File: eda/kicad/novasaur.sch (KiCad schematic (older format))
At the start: 30 parts, among them J9 RAM, SW1 RESET, U1 74F86, U10 74F574, U11 74F574, U12 ATF16V8B, U2 74F08, U3 74F32, U4 74ALS139, U5 74ALS139, U6 74F157, U7 74F175, U8 74F574, U9 74F138, X1 33M

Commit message: power sw + super caps
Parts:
- removed J9: RAM, Connector_PinHeader_2.54mm:PinHeader_1x03_P2.54mm_Vertical, symbol Connector_Generic:Conn_01x03
- removed R1: 1k, Resistor_THT:R_Axial_DIN0204_L3.6mm_D1.6mm_P7.62mm_Horizontal, symbol Device:R_US
- removed SW1: RESET, FSMRA3JH04:SWITCH_FSMRA3JH04, symbol novasaur-rescue:SW_Push-Switch
- TP28: value ILCP -> CLCP
- TP29: value IHCP -> CHCP
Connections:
- net DA17: now also U6.7 (Zb)
- net I0 renamed C0
- net I1 renamed C1
- net I10 renamed C10
- net I11 renamed C11
- net I12 renamed C12
- net I13 renamed C13
- net I14 renamed C14
- net I15 renamed C15
- net I2 renamed C2
- net I3 renamed C3
- net I4 renamed C4
- net I5 renamed C5
- net I6 renamed C6
- net I7 renamed C7
- net I8 renamed C8
- net I9 renamed C9
- net ccp renamed tcp
- net ~inoe renamed ~ioe
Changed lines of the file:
@@
 Sheet 1 4
 Title "Novasaur Retrocomputer"
-Date "2020-03-31"
+Date "2020-05-02"
 Rev "1.6"
 Comp ""
@@
 Wire Wire Line
 	4250 6000 4250 6550
-$Comp
-L novasaur-rescue:SW_Push-Switch SW1
-U 1 1 5E0603B4
-P 3650 1500
-AR Path="/5E0603B4" Ref="SW1"  Part="1"
-AR Path="/5CDEEC9F/5E0603B4" Ref="SW?"  Part="1"
-AR Path="/62D13D9D/5E0603B4" Ref="SW?"  Part="1"
-AR Path="/5DAA5CD8/5E0603B4" Ref="SW?"  Part="1"
-F 0 "SW1" H 3600 1850 50  0000 L CNN
-F 1 "RESET" H 3550 1750 50  0000 L CNN
-F 2 "FSMRA3JH04:SWITCH_FSMRA3JH04" H 3650 1700 50  0001 C CNN
-F 3 "~" H 3650 1700 50  0001 C CNN
-	1    3650 1500
-	-1   0    0    -1
-$EndComp
 Text GLabel 1350 1800 0    50   Output ~ 0
 alu
@@
 pcent
 Text Label 2500 1700 0    50   ~ 0
-I12
+C12
 Entry Wire Line
 	2650 1700 2750 1800
-Text GLabel 2750 1600 2    50   Input ~ 0
+Text GLabel 3050 1600 2    50   Input ~ 0
 DD[0..7]
 Wire Wire Line
@@
 $EndComp
 Text Label 2550 3200 0    50   ~ 0
-I8
+C8
 Text Label 2550 3300 0    50   ~ 0
-I9
+C9
 Text Label 2550 3400 0    50   ~ 0
-I0
+C0
 Text Label 2500 1900 0    50   ~ 0
-I14
+C14
 Text GLabel 2750 6000 3    50   Output ~ 0
-I[0..15]
+C[0..15]
 Entry Wire Line
 	2650 3200 2750 3300
@@
 	4450 5800 4350 5700
 Text Label 2550 5000 0    50   ~ 0
-I8
+C8
 Text Label 2550 5100 0    50   ~ 0
-I9
+C9
 Text Label 2500 5200 0    50   ~ 0
-I10
+C10
 Text Label 2500 5300 0    50   ~ 0
-I11
+C11
 Text Label 2500 5400 0    50   ~ 0
-I12
+C12
 Text Label 2500 5500 0    50   ~ 0
-I13
+C13
 Text Label 2500 5600 0    50   ~ 0
-I14
+C14
 Text Label 2500 5700 0    50   ~ 0
-I15
+C15
 Text Label 4200 5000 0    50   ~ 0
 PD0
@@
 	2650 1900 2750 2000
 Text Label 2500 1800 0    50   ~ 0
-I13
+C13
 Entry Wire Line
 	2650 1800 2750 1900
@@
 PD0
 Text Label 2850 5700 0    50   ~ 0
-I7
+C7
 Text Label 2850 5600 0    50   ~ 0
-I6
+C6
 Text Label 2850 5500 0    50   ~ 0
-I5
+C5
 Text Label 2850 5400 0    50   ~ 0
-I4
+C4
 Text Label 2850 5300 0    50   ~ 0
-I3
+C3
 Text Label 2850 5200 0    50   ~ 0
-I2
+C2
 Text Label 2850 5100 0    50   ~ 0
-I1
+C1
 Text Label 2850 5000 0    50   ~ 0
-I0
+C0
 Entry Wire Line
 	2750 5800 2650 5700
@@
 	1150 5000 1050 4900
 Text Label 2550 3700 0    50   ~ 0
-I1
+C1
 Text GLabel 1350 3900 0    50   Output ~ 0
 pgcp
@@
 $EndComp
 Text Label 2500 2000 0    50   ~ 0
-I15
+C15
 Entry Wire Line
 	2750 4650 2850 4550
@@
 	2850 4650 3050 4650
 Text Label 2850 4650 0    50   ~ 0
-I0
+C0
 Text Label 2850 4550 0    50   ~ 0
-I1
+C1
 Text Label 2850 4450 0    50   ~ 0
-I2
+C2
 Text Label 2850 4350 0    50   ~ 0
-I3
+C3
 Text Label 2850 4250 0    50   ~ 0
-I4
+C4
 Text Label 2850 4150 0    50   ~ 0
-I5
+C5
 Text Label 2850 4050 0    50   ~ 0
-I6
+C6
 Text Label 2850 3950 0    50   ~ 0
-I7
+C7
 $Comp
 L power:VCC #PWR?
@@
 ~exec
 Text GLabel 9300 1700 2    50   Output ~ 0
-ccp
+tcp
 Text GLabel 6900 2300 0    50   Input ~ 0
 hblank
@@
 	1    0    0    -1
 $EndComp
-$Comp
-L power:GNDD #PWR?
-U 1 1 5DEF95A1
-P 4150 1650
-AR Path="/5CDEEC9F/5DEF95A1" Ref="#PWR?"  Part="1"
-AR Path="/5DAA5CD8/5DEF95A1" Ref="#PWR?"  Part="1"
-AR Path="/5DEF95A1" Ref="#PWR0194"  Part="1"
-F 0 "#PWR0194" H 4150 1400 50  0001 C CNN
-F 1 "GNDD" H 4154 1495 50  0000 C CNN
-F 2 "" H 4150 1650 50  0001 C CNN
-F 3 "" H 4150 1650 50  0001 C CNN
-	1    4150 1650
-	1    0    0    -1
-$EndComp
-Wire Wire Line
-	4150 1550 4150 1650
-Wire Wire Line
-	4000 1600 4000 1550
-Wire Wire Line
-	4000 1500 3950 1500
-Wire Wire Line
-	4000 1550 4150 1550
-Connection ~ 4000 1550
-Wire Wire Line
-	4000 1550 4000 1500
-Text Label 2500 1600 0    50   ~ 0
+Text Label 2850 1600 0    50   ~ 0
 DD7
-$Comp
-L Device:R_US R?
-U 1 1 5E523FD1
-P 3050 1300
-AR Path="/62D13D9D/5E523FD1" Ref="R?"  Part="1"
-AR Path="/5DAA19D5/5E523FD1" Ref="R?"  Part="1"
-AR Path="/5DAA5CD8/5D99DA9F/5E523FD1" Ref="R?"  Part="1"
-AR Path="/5DA1E9BA/5E523FD1" Ref="R?"  Part="1"
-AR Path="/5E523FD1" Ref="R1"  Part="1"
-F 0 "R1" H 3150 1350 50  0000 L CNN
-F 1 "1k" H 3150 1250 50  0000 L CNN
-F 2 "Resistor_THT:R_Axial_DIN0204_L3.6mm_D1.6mm_P7.62mm_Horizontal" V 3090 1290 50  0001 C CNN
-F 3 "~" H 3050 1300 50  0001 C CNN
-	1    3050 1300
-	1    0    0    -1
-$EndComp
-$Comp
-L power:VCC #PWR?
-U 1 1 5E54FDAD
-P 3050 1100
-AR Path="/5CDEEC9F/5E54FDAD" Ref="#PWR?"  Part="1"
-AR Path="/5DAA5CD8/5E54FDAD" Ref="#PWR?"  Part="1"
-AR Path="/5E54FDAD" Ref="#PWR0111"  Part="1"
-F 0 "#PWR0111" H 3050 950 50  0001 C CNN
-F 1 "VCC" H 3067 1273 50  0000 C CNN
-F 2 "" H 3050 1100 50  0001 C CNN
-F 3 "" H 3050 1100 50  0001 C CNN
-	1    3050 1100
-	1    0    0    -1
-$EndComp
-Wire Wire Line
-	3050 1500 3050 1450
-Wire Wire Line
-	3050 1150 3050 1100
 Wire Wire Line
 	9600 1100 8000 1100
@@
 	2850 3200 3150 3200
 Text Label 2850 3100 0    50   ~ 0
-I3
+C3
 Text GLabel 3150 3400 0    50   Input ~ 0
 ~read
@@
 acp
 Text GLabel 4150 3100 2    50   Output ~ 0
-~inoe
+~ioe
 Entry Wire Line
 	2850 2200 2750 2300
 Text Label 2850 2200 0    50   ~ 0
-I13
+C13
 Text Label 2850 3200 0    50   ~ 0
-I12
+C12
 Entry Wire Line
 	2850 3100 2750 3200
@@
 $EndSheet
 Text Label 2850 3700 0    50   ~ 0
-I2
+C2
 Entry Wire Line
 	2850 3700 2750 3800
@@
 	2850 2600 2750 2700
 Text Label 2850 2600 0    50   ~ 0
-I10
+C10
 Wire Wire Line
 	2850 2600 4450 2600
@@
 	2850 1900 2750 2000
 Text Label 2850 1900 0    50   ~ 0
-I11
+C11
 Wire Wire Line
 	2850 2200 4450 2200
@@
 $EndComp
 Wire Wire Line
-	3950 1600 4000 1600
-Wire Wire Line
 	7600 4650 7500 4650
 Connection ~ 7600 4650
-Text GLabel 6850 3000 0    50   Output ~ 0
+Text GLabel 6600 3100 2    50   Output ~ 0
 DA17
 Wire Wire Line
@@
 	2850 3700 4200 3700
 Wire Wire Line
-	2750 1600 2350 1600
-Connection ~ 3050 1500
-Wire Wire Line
-	2350 1500 2850 1500
-Wire Wire Line
 	4200 3700 4200 4000
-$Comp
-L Connector_Generic:Conn_01x03 J?
-U 1 1 5E60D57E
-P 7050 3000
-AR Path="/5DA1E9C0/5E60D57E" Ref="J?"  Part="1"
-AR Path="/5E60D57E" Ref="J9"  Part="1"
-F 0 "J9" H 7000 3350 50  0000 L CNN
-F 1 "RAM" H 6950 3250 50  0000 L CNN
-F 2 "Connector_PinHeader_2.54mm:PinHeader_1x03_P2.54mm_Vertical" H 7050 3000 50  0001 C CNN
-F 3 "~" H 7050 3000 50  0001 C CNN
-	1    7050 3000
-	1    0    0    -1
-$EndComp
-Wire Wire Line
-	6600 3100 6850 3100
-Text GLabel 6850 2900 0    50   Input ~ 0
-1
 $Comp
 L Connector:TestPoint_Alt TP29
@@
 AR Path="/5DA1E9C0/5E51CAB2" Ref="TP?"  Part="1"
 F 0 "TP29" H 1100 6000 50  0000 L CNN
-F 1 "IHCP" H 1100 6050 50  0001 L CNN
+F 1 "CHCP" H 1100 6050 50  0001 L CNN
 F 2 "TestPoint:TestPoint_Pad_1.0x1.0mm" H 1550 5900 50  0001 C CNN
 F 3 "~" H 1550 5900 50  0001 C CNN
@@
 	5600 5900 4150 5900
 Connection ~ 4150 5900
-Text GLabel 2850 1400 1    50   Input ~ 0
+Text GLabel 2350 1500 2    50   Input ~ 0
 ~reset
-Wire Wire Line
-	3050 1500 3350 1500
-Wire Wire Line
-	2850 1400 2850 1500
-Connection ~ 2850 1500
-Wire Wire Line
-	2850 1500 3050 1500
-Wire Bus Line
-	4450 5100 4450 6750
-Wire Bus Line
-	1050 4700 1050 6750
-Wire Bus Line
-	2750 1800 2750 6000
 $Comp
 L Connector:TestPoint_Alt TP28
@@
 AR Path="/5DA1E9C0/5E514E07" Ref="TP?"  Part="1"
 F 0 "TP28" H 4200 6000 50  0000 L CNN
-F 1 "ILCP" H 3900 6050 50  0001 L CNN
+F 1 "CLCP" H 3900 6050 50  0001 L CNN
 F 2 "TestPoint:TestPoint_Pad_1.0x1.0mm" H 4350 5900 50  0001 C CNN
 F 3 "~" H 4350 5900 50  0001 C CNN
@@
 	1    0    0    -1
 $EndComp
+Wire Wire Line
+	2350 1600 3050 1600
+Wire Bus Line
+	4450 5100 4450 6750
+Wire Bus Line
+	1050 4700 1050 6750
+Wire Bus Line
+	2750 1800 2750 6000
 $EndSCHEMATC

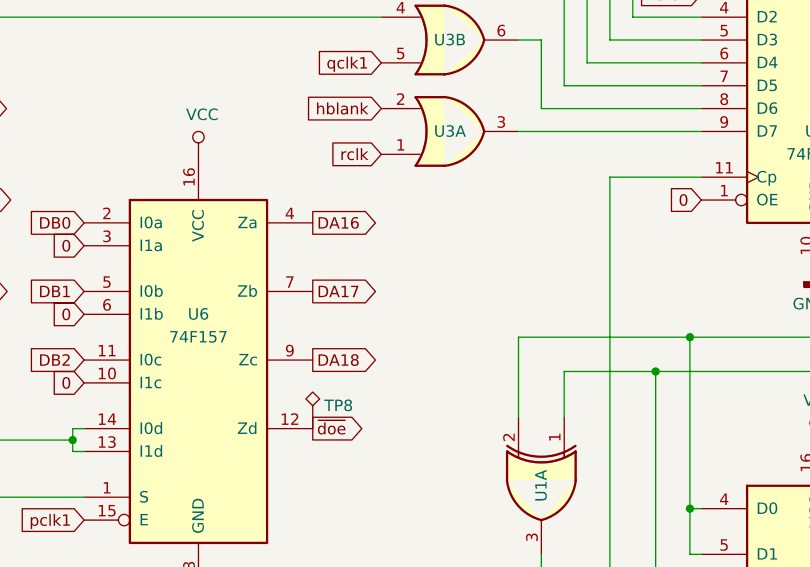
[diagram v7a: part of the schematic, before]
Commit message: update sw footprint
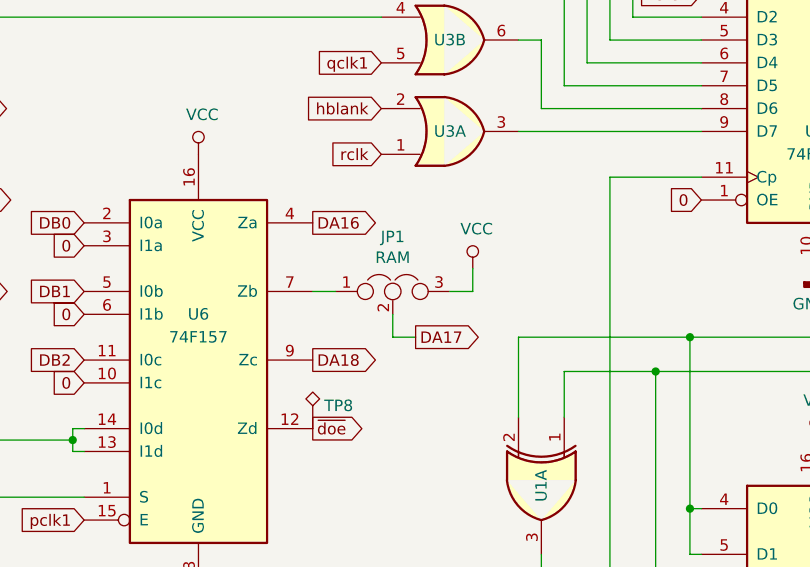
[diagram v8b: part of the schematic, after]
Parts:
- added JP1: RAM, Jumper:SolderJumper-3_P1.3mm_Bridged2Bar12_Pad1.0x1.5mm_NumberLabels, symbol Device:Jumper_NC_Dual
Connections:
- net DA17: now also JP1.2; no longer U6.7 (Zb)
- net VCC: now also JP1.3
- new net: JP1.1, U6.7 (Zb)
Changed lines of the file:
@@
 	7600 4650 7500 4650
 Connection ~ 7600 4650
-Text GLabel 6600 3100 2    50   Output ~ 0
+Text GLabel 7050 3300 2    50   Output ~ 0
 DA17
 Wire Wire Line
@@
 Wire Wire Line
 	2350 1600 3050 1600
+$Comp
+L Device:Jumper_NC_Dual JP1
+U 1 1 5EAEF12E
+P 6950 3100
+F 0 "JP1" H 6950 3339 50  0000 C CNN
+F 1 "RAM" H 6950 3248 50  0000 C CNN
+F 2 "Jumper:SolderJumper-3_P1.3mm_Bridged2Bar12_Pad1.0x1.5mm_NumberLabels" H 6950 3100 50  0001 C CNN
+F 3 "~" H 6950 3100 50  0001 C CNN
+	1    6950 3100
+	1    0    0    -1
+$EndComp
+Wire Wire Line
+	7050 3300 6950 3300
+Wire Wire Line
+	6950 3300 6950 3200
+$Comp
+L power:VCC #PWR?
+U 1 1 5EAF98E7
+P 7300 3000
+AR Path="/5CDEEC9F/5EAF98E7" Ref="#PWR?"  Part="1"
+AR Path="/5DAA5CD8/5EAF98E7" Ref="#PWR?"  Part="1"
+AR Path="/5EAF98E7" Ref="#PWR0198"  Part="1"
+F 0 "#PWR0198" H 7300 2850 50  0001 C CNN
+F 1 "VCC" H 7317 3173 50  0000 C CNN
+F 2 "" H 7300 3000 50  0001 C CNN
+F 3 "" H 7300 3000 50  0001 C CNN
+	1    7300 3000
+	1    0    0    -1
+$EndComp
+Wire Wire Line
+	7200 3100 7300 3100
+Wire Wire Line
+	7300 3100 7300 3000
+Wire Wire Line
+	6600 3100 6700 3100
 Wire Bus Line
 	4450 5100 4450 6750
